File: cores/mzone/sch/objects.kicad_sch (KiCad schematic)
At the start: 36 parts

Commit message: mzone core
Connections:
- net AB''4 renamed MA'4
- net AB''5 renamed MA'5
- net AB''6 renamed MA'6
- net AB''7 renamed MA'7
- net AB''8 renamed MA'8
- net AB''9 renamed MA'9
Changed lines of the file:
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@@
 		)
 	)
-	(label "AB''7"
+	(label "MA'7"
 		(at 19.05 199.39 0)
 		(effects
@@
 		)
 	)
-	(label "AB''0"
+	(label "MA'0"
 		(at 19.05 248.92 0)
 		(effects
@@
 		)
 	)
-	(label "AB''2"
+	(label "MA'2"
 		(at 19.05 246.38 0)
 		(effects
@@
 		)
 	)
-	(label "AB''3"
+	(label "MA'3"
 		(at 19.05 241.3 0)
 		(effects
@@
 		)
 	)
-	(label "AB''8"
+	(label "MA'8"
 		(at 29.21 271.78 0)
 		(effects
@@
 		)
 	)
-	(label "AB''1"
+	(label "MA'1"
 		(at 19.05 243.84 0)
 		(effects
@@
 		)
 	)
-	(label "AB''5"
+	(label "MA'5"
 		(at 19.05 204.47 0)
 		(effects
@@
 		)
 	)
-	(label "AB''6"
+	(label "MA'6"
 		(at 19.05 196.85 0)
 		(effects
@@
 		)
 	)
-	(label "AB''4"
+	(label "MA'4"
 		(at 19.05 201.93 0)
 		(effects
@@
 		)
 	)
-	(label "AB''9"
+	(label "MA'9"
 		(at 29.21 264.16 0)
 		(effects

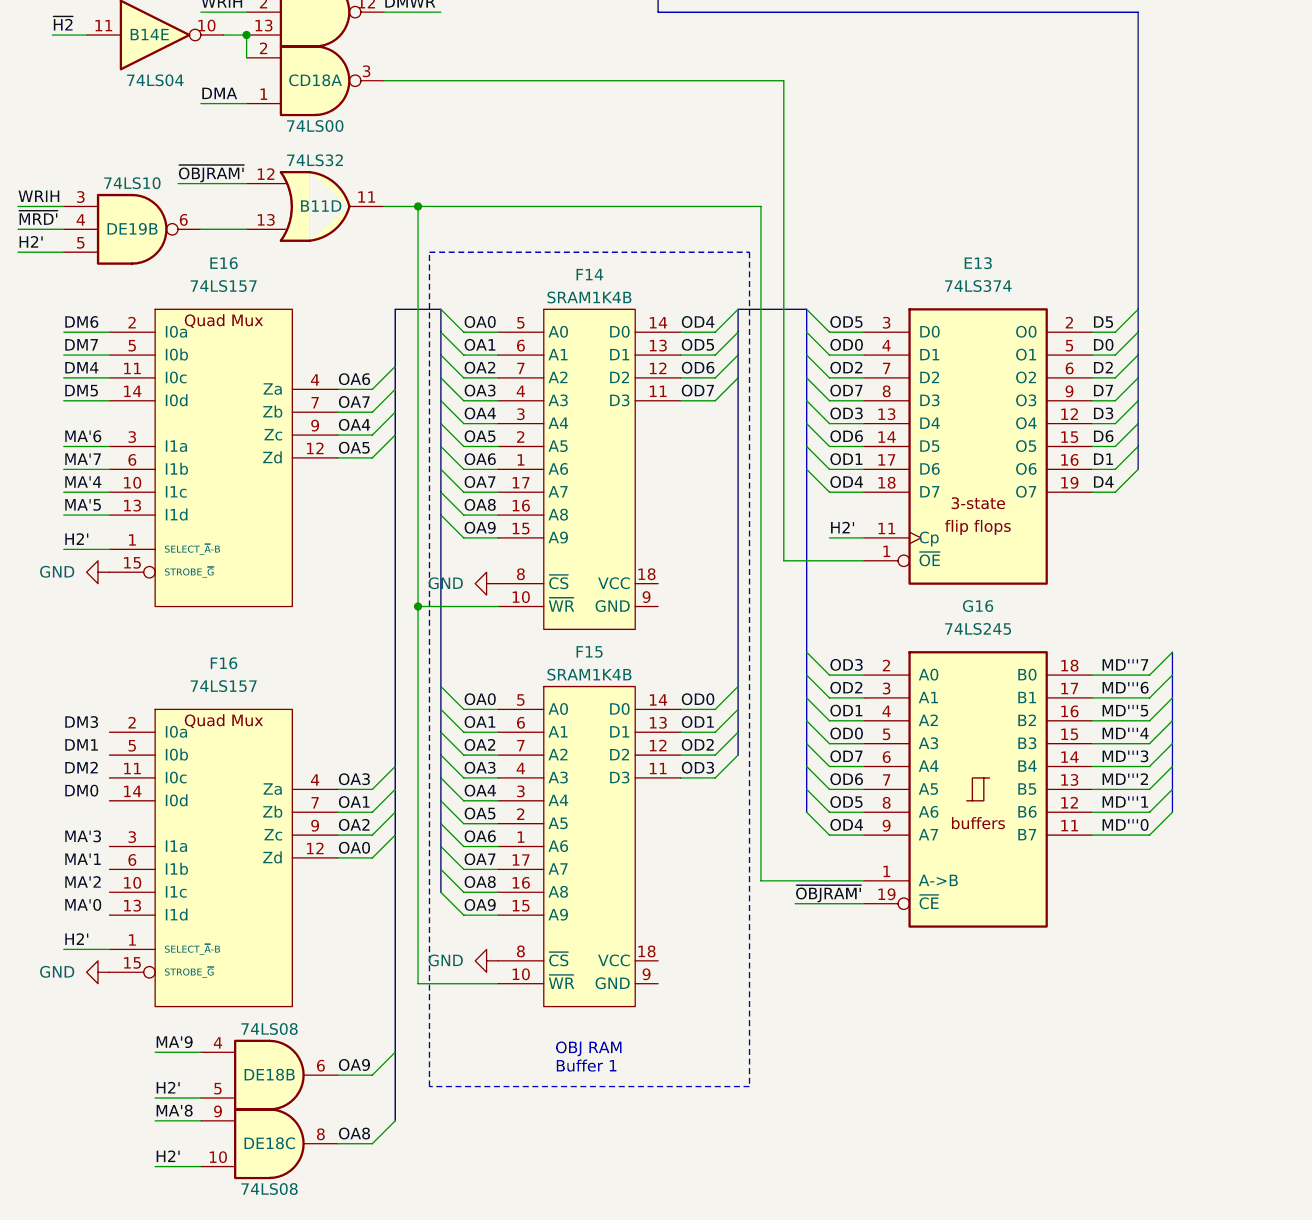
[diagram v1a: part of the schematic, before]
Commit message: mzone core
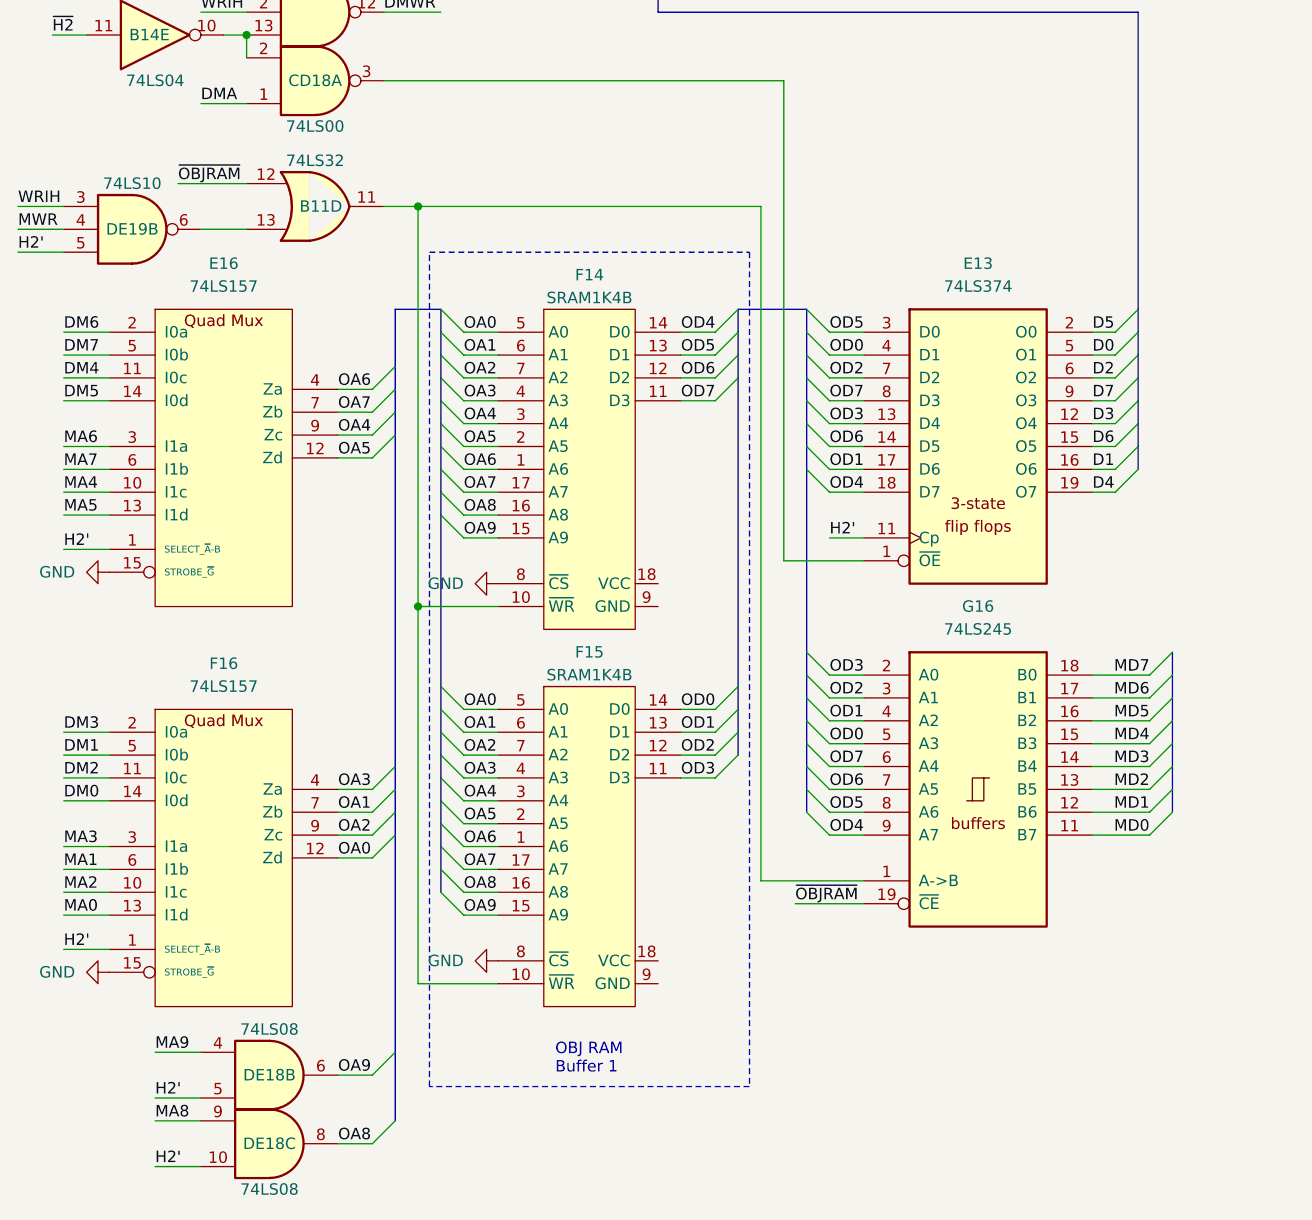
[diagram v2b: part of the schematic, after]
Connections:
- net DM0: now also F16.14 (I0d)
- net DM1: now also F16.5 (I0b)
- net DM2: now also F16.11 (I0c)
- net DM3: now also F16.2 (I0a)
- net MA2: now reaches F16.10 (I1c)
- net MA0: now reaches F16.13 (I1d)
- net MA3: now reaches F16.3 (I1a)
- net MA1: now reaches F16.6 (I1b)
- net MA'4 renamed MA4
- net MA'5 renamed MA5
- net MA'6 renamed MA6
- net MA'7 renamed MA7
- net MA'8 renamed MA8
- net MA'9 renamed MA9
- net MD'''0 renamed MD0
- net MD'''1 renamed MD1
- net MD'''2 renamed MD2
- net MD'''3 renamed MD3
- net MD'''4 renamed MD4
- net MD'''5 renamed MD5
- net MD'''6 renamed MD6
- net MD'''7 renamed MD7
- net ~{MRD'} renamed MWR
- net ~{OBJRAM'} renamed ~{OBJRAM}
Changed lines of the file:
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@@
 		)
 	)
+	(wire
+		(pts
+			(xy 19.05 246.38) (xy 24.13 246.38)
+		)
+		(stroke
+			(width 0)
+			(type default)
+		)
+	)
 	(bus
 		(pts
@@
 	(wire
 		(pts
+			(xy 19.05 228.6) (xy 24.13 228.6)
+		)
+		(stroke
+			(width 0)
+			(type default)
+		)
+	)
+	(wire
+		(pts
 			(xy 326.39 58.42) (xy 332.74 58.42)
 		)
@@
 	(wire
 		(pts
+			(xy 19.05 233.68) (xy 24.13 233.68)
+		)
+		(stroke
+			(width 0)
+			(type default)
+		)
+	)
+	(wire
+		(pts
 			(xy 212.09 259.08) (xy 219.71 259.08)
 		)
@@
 		)
 	)
+	(wire
+		(pts
+			(xy 19.05 248.92) (xy 24.13 248.92)
+		)
+		(stroke
+			(width 0)
+			(type default)
+		)
+	)
 	(bus
 		(pts
@@
 	(wire
 		(pts
+			(xy 19.05 236.22) (xy 24.13 236.22)
+		)
+		(stroke
+			(width 0)
+			(type default)
+		)
+	)
+	(wire
+		(pts
 			(xy 368.3 118.11) (xy 374.65 118.11)
 		)
@@
 	(wire
 		(pts
+			(xy 19.05 231.14) (xy 24.13 231.14)
+		)
+		(stroke
+			(width 0)
+			(type default)
+		)
+	)
+	(wire
+		(pts
 			(xy 350.52 58.42) (xy 350.52 60.96)
 		)
@@
 		)
 	)
+	(wire
+		(pts
+			(xy 19.05 241.3) (xy 24.13 241.3)
+		)
+		(stroke
+			(width 0)
+			(type default)
+		)
+	)
 	(bus
 		(pts
@@
 	(wire
 		(pts
+			(xy 19.05 243.84) (xy 24.13 243.84)
+		)
+		(stroke
+			(width 0)
+			(type default)
+		)
+	)
+	(wire
+		(pts
 			(xy 104.14 186.69) (xy 107.95 186.69)
 		)
@@
 		)
 	)
-	(label "~{OBJRAM'}"
+	(label "~{OBJRAM}"
 		(at 31.75 167.64 0)
 		(effects
@@
 		)
 	)
-	(label "MD'''2"
+	(label "MD2"
 		(at 139.7 234.95 180)
 		(effects
@@
 		)
 	)
-	(label "~{MRD'}"
+	(label "MWR"
 		(at 13.97 172.72 0)
 		(effects
@@
 		)
 	)
-	(label "MD'''5"
+	(label "MD5"
 		(at 139.7 227.33 180)
 		(effects
@@
 		)
 	)
-	(label "MD'''4"
+	(label "MD4"
 		(at 139.7 229.87 180)
 		(effects
@@
 		)
 	)
-	(label "MD'''3"
+	(label "MD3"
 		(at 139.7 232.41 180)
 		(effects
@@
 		)
 	)
-	(label "MD'''6"
+	(label "MD6"
 		(at 139.7 224.79 180)
 		(effects
@@
 		)
 	)
-	(label "MD'''7"
+	(label "MD7"
 		(at 139.7 222.25 180)
 		(effects
@@
 		)
 	)
-	(label "MA'7"
+	(label "MA7"
 		(at 19.05 199.39 0)
 		(effects
@@
 		)
 	)
-	(label "MA'0"
+	(label "MA0"
 		(at 19.05 248.92 0)
 		(effects
@@
 		)
 	)
-	(label "MA'2"
+	(label "MA2"
 		(at 19.05 246.38 0)
 		(effects
@@
 		)
 	)
-	(label "MD'''0"
+	(label "MD0"
 		(at 139.7 240.03 180)
 		(effects
@@
 		)
 	)
-	(label "~{OBJRAM'}"
+	(label "~{OBJRAM}"
 		(at 100.33 247.65 0)
 		(effects
@@
 		)
 	)
-	(label "MA'3"
+	(label "MA3"
 		(at 19.05 241.3 0)
 		(effects
@@
 		)
 	)
-	(label "MA'8"
+	(label "MA8"
 		(at 29.21 271.78 0)
 		(effects
@@
 		)
 	)
-	(label "MA'1"
+	(label "MA1"
 		(at 19.05 243.84 0)
 		(effects
@@
 		)
 	)
-	(label "MA'5"
+	(label "MA5"
 		(at 19.05 204.47 0)
 		(effects
@@
 		)
 	)
-	(label "MA'6"
+	(label "MA6"
 		(at 19.05 196.85 0)
 		(effects
@@
 		)
 	)
-	(label "MA'4"
+	(label "MA4"
 		(at 19.05 201.93 0)
 		(effects
@@
 		)
 	)
-	(label "MA'9"
+	(label "MA9"
 		(at 29.21 264.16 0)
 		(effects
@@
 		)
 	)
-	(label "MD'''1"
+	(label "MD1"
 		(at 139.7 237.49 180)
 		(effects

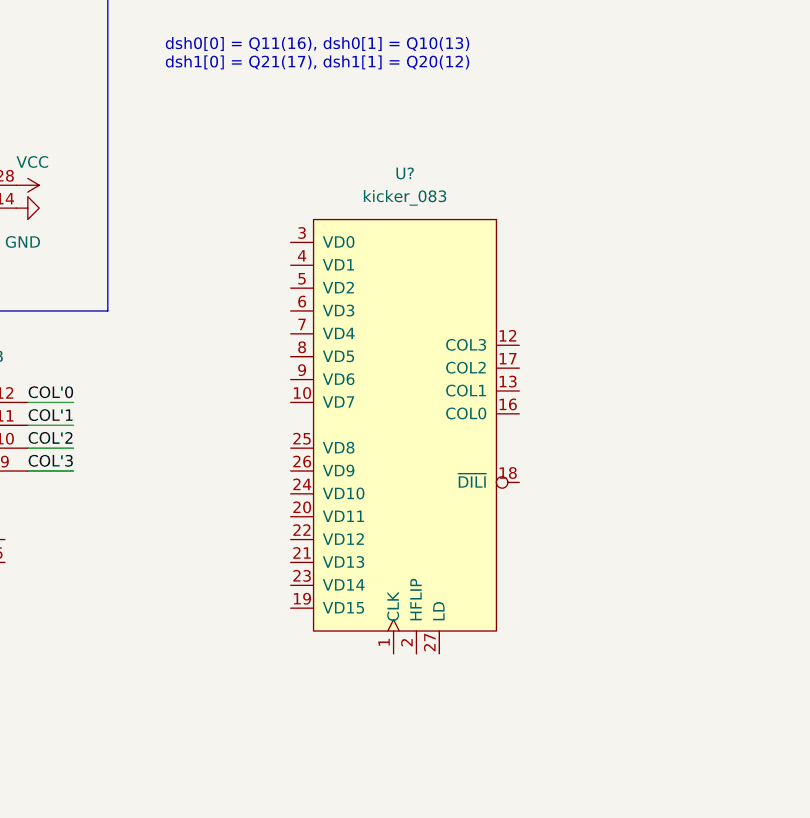
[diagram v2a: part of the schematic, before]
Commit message: mzone core
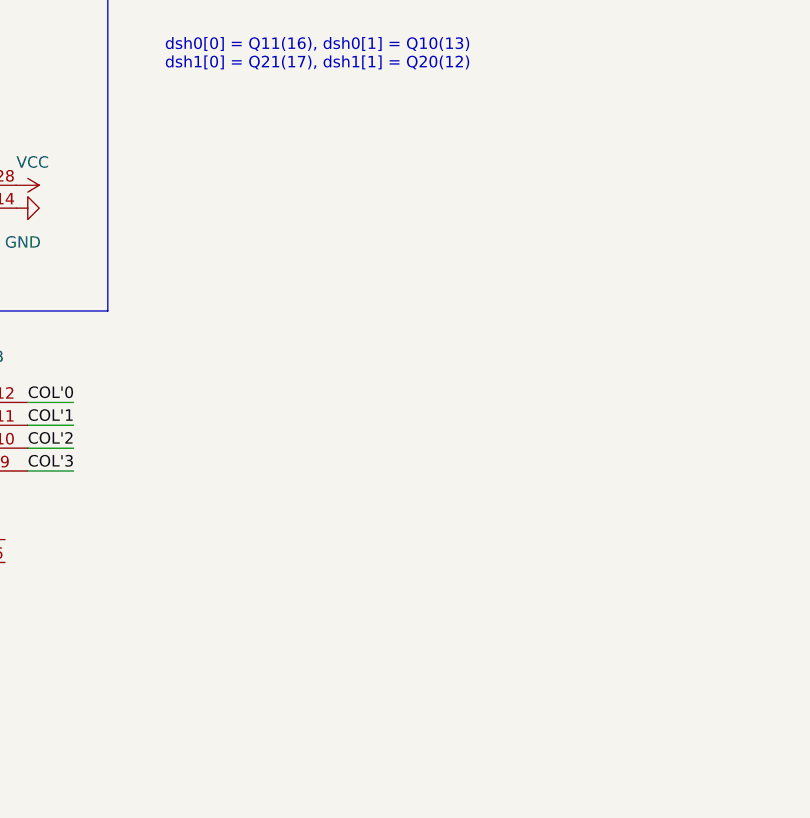
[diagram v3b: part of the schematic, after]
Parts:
- removed U?: kicker_083, symbol konami:kicker_083
